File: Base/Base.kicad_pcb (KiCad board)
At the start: 2 copper layers, 23 parts, among them P1 CONN_01X02, P2 CONN_01X05, P3 CONN_01X08, P4 CONN_01X08, Q1 FDC606P, U1 tps610981, U2 M24M01, U4 CYBLE-022001-00

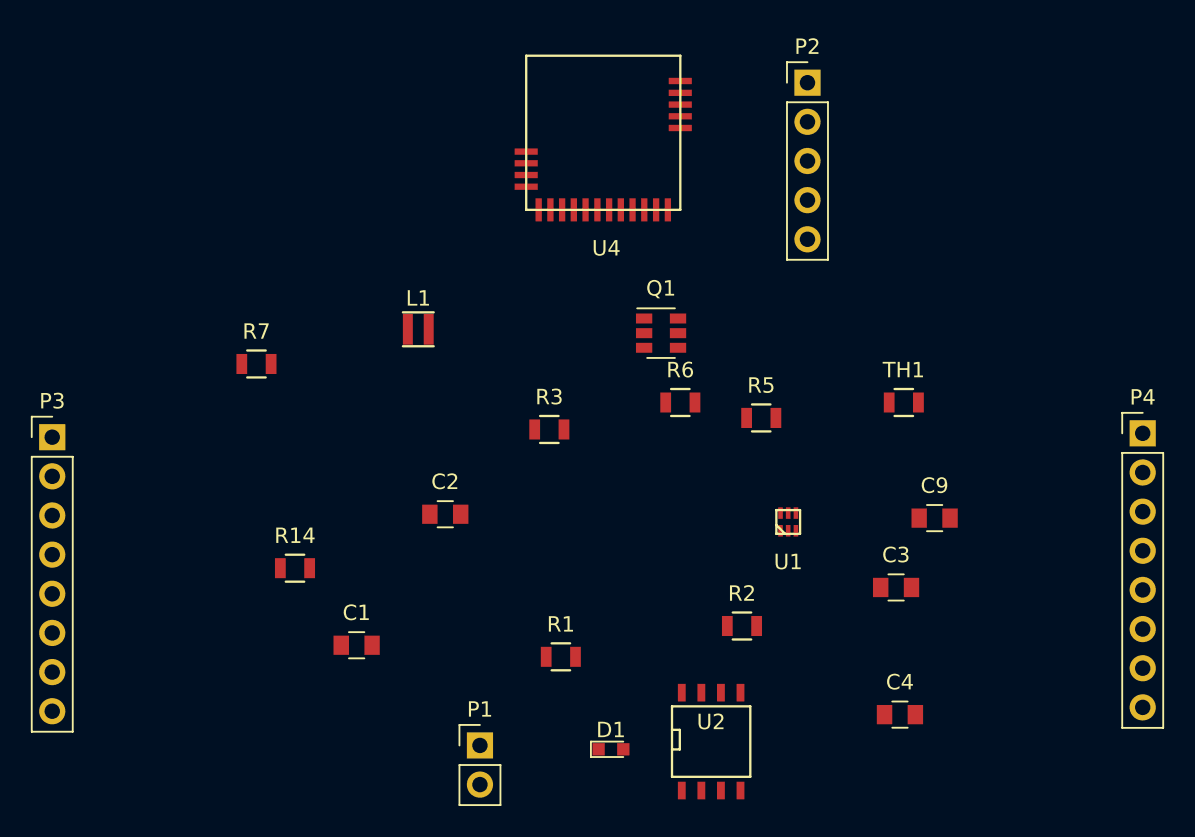
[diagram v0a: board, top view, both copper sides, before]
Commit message: Working on the layout for the base station.
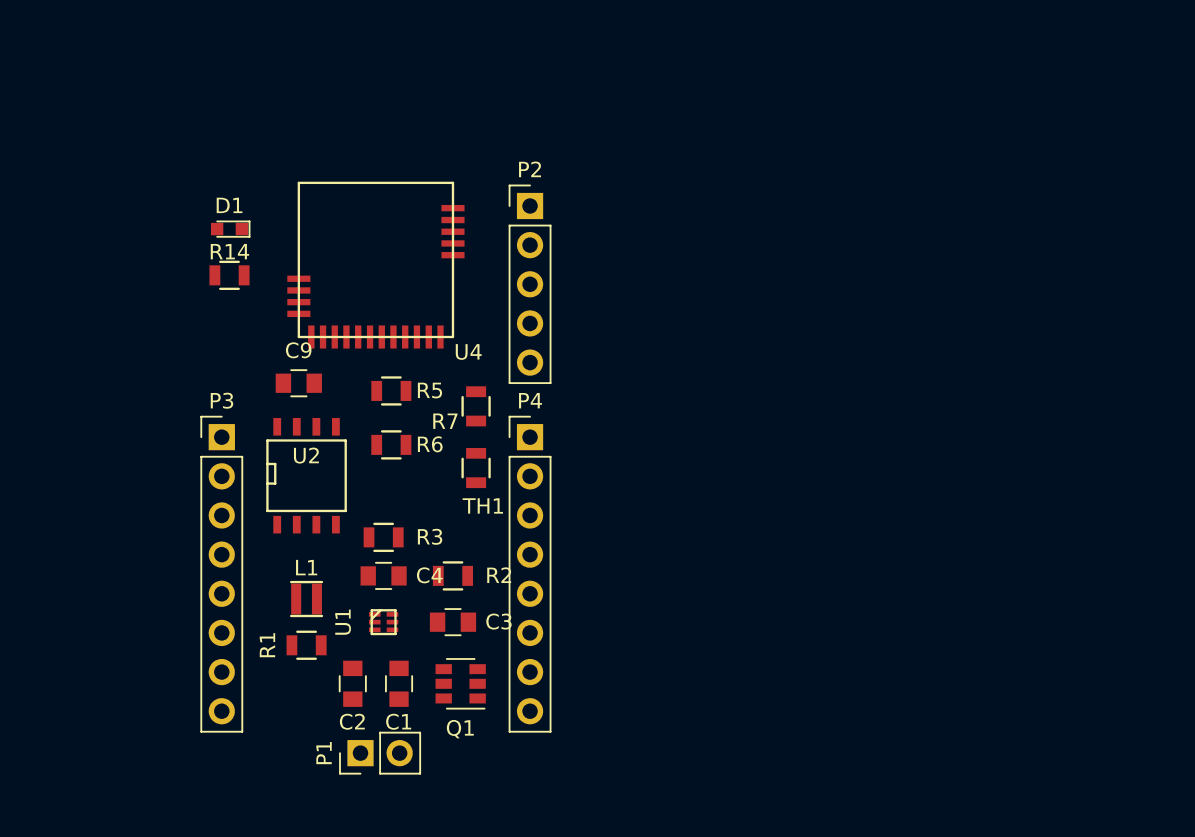
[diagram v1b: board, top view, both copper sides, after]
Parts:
- moved C9 42.2 mm to (124.0, 98.5)
- moved D1 41.9 mm to (119.5, 88.5), turned to 180 degrees
- moved P4 39.8 mm to (139.0, 102.0)
- moved C4 34.7 mm to (129.5, 111.0)
- moved U2 31.4 mm to (124.5, 104.5)
- moved C3 28.8 mm to (134.0, 114.0)
- moved TH1 28.1 mm to (135.5, 104.0), turned to 270 degrees
- moved U1 27.0 mm to (129.5, 114.0), turned to 270 degrees
- moved Q1 26.2 mm to (134.5, 118.0), turned to 180 degrees
- moved R5 24.1 mm to (130.0, 99.0), turned to 180 degrees
- moved P2 19.7 mm to (139.0, 87.0)
- moved R14 19.5 mm to (119.5, 91.5)
- moved R2 19.0 mm to (134.0, 111.0), turned to 180 degrees
- moved R6 19.0 mm to (130.0, 102.5), turned to 180 degrees
- moved L1 18.9 mm to (124.5, 112.5)
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
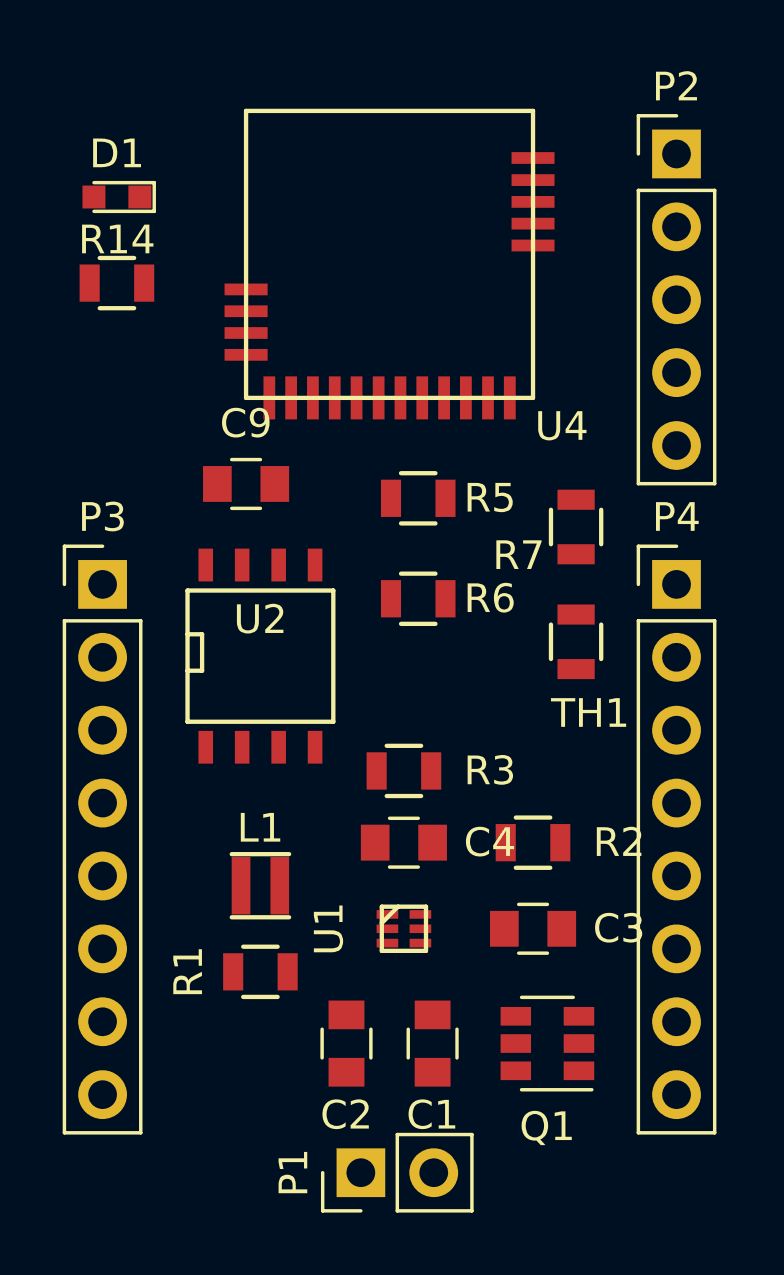
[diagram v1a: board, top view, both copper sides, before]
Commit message: Completed the routing.
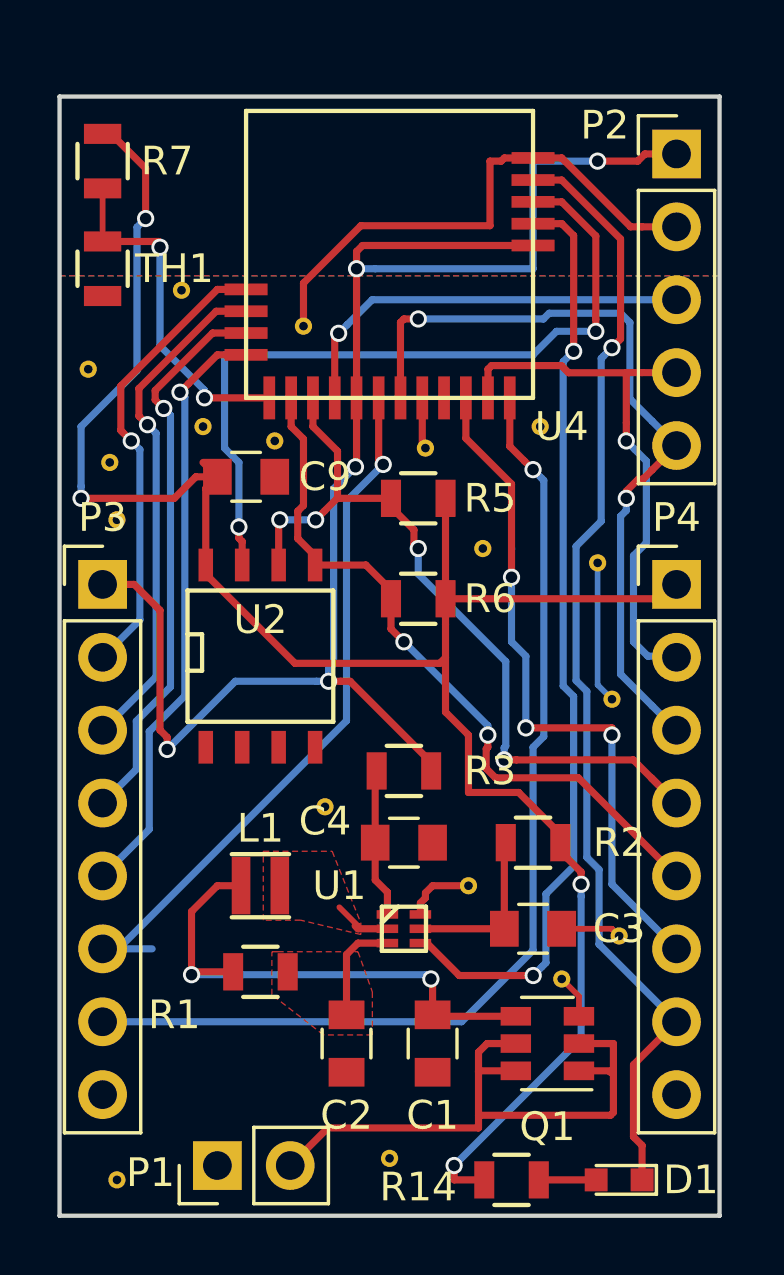
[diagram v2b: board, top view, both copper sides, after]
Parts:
- added REF**: via_0.3mm, KicadFootprint:via_0.3mm, F.Cu at (119.5, 99.8)
- added REF**: via_0.3mm, KicadFootprint:via_0.3mm, F.Cu at (136.2, 101.2)
- added REF**: via_0.3mm, KicadFootprint:via_0.3mm, F.Cu at (136.8, 106.0)
- added REF**: via_0.3mm, KicadFootprint:via_0.3mm, F.Cu at (132.2, 100.8)
- added REF**: via_0.3mm, KicadFootprint:via_0.3mm, F.Cu at (126.8, 109.8)
- added REF**: via_0.3mm, KicadFootprint:via_0.3mm, F.Cu at (137.0, 114.2)
- added REF**: via_0.3mm, KicadFootprint:via_0.3mm, F.Cu at (131.8, 112.5)
- added REF**: via_0.3mm, KicadFootprint:via_0.3mm, F.Cu at (135.0, 115.8)
- added REF**: via_0.3mm, KicadFootprint:via_0.3mm, F.Cu at (129.0, 122.0)
- added REF**: via_0.3mm, KicadFootprint:via_0.3mm, F.Cu at (119.5, 122.8)
- added REF**: via_0.3mm, KicadFootprint:via_0.3mm, F.Cu at (119.2, 97.8)
- added REF**: via_0.3mm, KicadFootprint:via_0.3mm, F.Cu at (121.8, 91.8)
- added REF**: via_0.3mm, KicadFootprint:via_0.3mm, F.Cu at (134.2, 96.5)
- added REF**: via_0.3mm, KicadFootprint:via_0.3mm, F.Cu at (126.0, 93.0)
- added REF**: via_0.3mm, KicadFootprint:via_0.3mm, F.Cu at (122.5, 96.5)
- added REF**: via_0.3mm, KicadFootprint:via_0.3mm, F.Cu at (125.0, 97.0)
- added REF**: via_0.3mm, KicadFootprint:via_0.3mm, F.Cu at (118.5, 94.5)
- added REF**: via_0.3mm, KicadFootprint:via_0.3mm, F.Cu at (130.2, 97.2)
- moved D1 38.5 mm to (137.0, 122.8)
- moved R14 34.1 mm to (133.2, 122.8), turned to 180 degrees
- moved TH1 21.0 mm to (119.0, 91.0)
- moved R7 20.9 mm to (119.0, 87.2)
- moved P1 5.01 mm to (123.0, 122.2)
- moved C9 0.25 mm to (124.0, 98.2)
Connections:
- P3 pad 2: /SWDIO -> /GPIO1
- P3 pad 3: /SWDCLK -> /ANALOG1
- P3 pad 4: /RX.MOSI -> /TX/MISO
- P3 pad 5: /TX/MISO -> /RX/MOSI
- P3 pad 6: /SS -> /SCLK
- P3 pad 7: /SCLK -> /SS
- P4 pad 2: /SDA -> /SWDCLK
- P4 pad 3: /SCL -> /SWDIO
- P4 pad 4: /ANALOG1 -> /SCL
- P4 pad 5: /ANALOG2 -> /SDA
- P4 pad 6: /GPIO1 -> /ANALOG2
- R7 pad 2: /ANALOG2 -> /TEMP
- TH1 pad 1: /ANALOG2 -> /TEMP
- U4 pad 17: /ANALOG2 -> /TEMP
- U4 pad 8: /GPIO2 -> /ANALOG2
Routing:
- net VDD: track 0.00 -> 71.6 mm, vias 0 -> 4
- net VCC: track 0.00 -> 55.7 mm, vias 0 -> 5
- net /LED: track 0.00 -> 39.5 mm, vias 0 -> 1
- net /SS: track 0.00 -> 35.9 mm, vias 0 -> 1
- net /PS_MODE: track 0.00 -> 32.7 mm, vias 0 -> 2
- net GND: track 0.00 -> 31.4 mm
- net /SWDIO: track 0.00 -> 27.5 mm, vias 0 -> 2
- net /SCL: track 0.00 -> 27.4 mm, vias 0 -> 4
- net /WP: track 0.00 -> 27.2 mm, vias 0 -> 2
- net /SDA: track 0.00 -> 25.5 mm, vias 0 -> 2
- net /SCLK: track 0.00 -> 25.4 mm, vias 0 -> 1
- net /ANALOG2: track 0.00 -> 24.0 mm, vias 0 -> 3
- net Net-(P1-Pad2): track 0.00 -> 22.2 mm
- net /RX/MOSI: track 0.00 -> 21.5 mm, vias 0 -> 1
- net /TX/MISO: track 0.00 -> 19.6 mm, vias 0 -> 1
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- added copper zone on B.Cu, net GND
- added copper zone on F.Cu, net GND
- added copper zone on F.Cu, net Net-(C2-Pad1)
- added copper zone on F.Cu, net Net-(L1-Pad2)
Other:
- board outline added: 23 x 39 mm
- net class Default: trace_width 0.25 -> 0.2

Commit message: Changing from a thermister ST LPS22HB pressure sensor.
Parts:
- removed R7: 10K, Resistors_SMD:R_0805
- removed the REF** at (119.5, 99.8)
- removed the REF** at (136.2, 101.2)
- removed the REF** at (136.8, 106.0)
- removed the REF** at (132.2, 100.8)
- removed the REF** at (126.8, 109.8)
- removed the REF** at (137.0, 114.2)
- removed the REF** at (131.8, 112.5)
- removed the REF** at (135.0, 115.8)
- removed the REF** at (129.0, 122.0)
- removed the REF** at (119.5, 122.8)
- removed the REF** at (119.2, 97.8)
- removed the REF** at (121.8, 91.8)
- removed the REF** at (134.2, 96.5)
- removed the REF** at (126.0, 93.0)
- removed the REF** at (122.5, 96.5)
- removed the REF** at (125.0, 97.0)
- removed the REF** at (118.5, 94.5)
- removed the REF** at (130.2, 97.2)
- removed TH1: Thermistor, Resistors_SMD:R_0805
- added REF**: via_0.3mm, KicadFootprint:via_0.3mm, F.Cu at (119.5, 92.0)
- added U3: LPS22HB, KicadFootprint:HLGA-10L, F.Cu at (120.5, 87.8)
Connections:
- U4 pad 17: /TEMP -> /INT_DRDY
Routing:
- net GND: track 31.4 -> 7.87 mm
- net /INT_DRDY: track 0.00 -> 18.0 mm, vias 0 -> 2
- net /TEMP: track 12.2 -> 0.00 mm, vias 2 -> 0
- net /SDA: track 25.5 -> 37.2 mm, vias 2 -> 4
- net /SCL: track 27.4 -> 38.4 mm, vias 4 -> 6
- net VDD: track 71.6 -> 79.5 mm
- net (no net): track 0.01 -> 4.97 mm

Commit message: Finished layout of SensorNode and FlowMeter boards.
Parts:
- added REF**: via_0.3mm, KicadFootprint:via_0.3mm, F.Cu at (132.2, 106.0)
- added REF**: via_0.3mm, KicadFootprint:via_0.3mm, F.Cu at (123.5, 104.5)
- added REF**: via_0.3mm, KicadFootprint:via_0.3mm, F.Cu at (137.0, 88.2)
- added REF**: via_0.3mm, KicadFootprint:via_0.3mm, F.Cu at (130.2, 97.2)
- added REF**: via_0.3mm, KicadFootprint:via_0.3mm, F.Cu at (124.0, 96.8)
- added REF**: via_0.3mm, KicadFootprint:via_0.3mm, F.Cu at (118.5, 87.5)
- added REF**: via_0.3mm, KicadFootprint:via_0.3mm, F.Cu at (121.5, 89.8)
- added REF**: via_0.3mm, KicadFootprint:via_0.3mm, F.Cu at (121.8, 86.2)
- added REF**: via_0.3mm, KicadFootprint:via_0.3mm, F.Cu at (132.2, 109.0)
- added REF**: via_0.3mm, KicadFootprint:via_0.3mm, F.Cu at (124.0, 119.2)
- added REF**: via_0.3mm, KicadFootprint:via_0.3mm, F.Cu at (129.0, 122.0)
- added REF**: via_0.3mm, KicadFootprint:via_0.3mm, F.Cu at (136.0, 121.2)
- added REF**: via_0.3mm, KicadFootprint:via_0.3mm, F.Cu at (137.0, 116.8)
- added REF**: via_0.3mm, KicadFootprint:via_0.3mm, F.Cu at (137.0, 113.8)
- added REF**: via_0.3mm, KicadFootprint:via_0.3mm, F.Cu at (132.0, 112.5)
- added REF**: via_0.3mm, KicadFootprint:via_0.3mm, F.Cu at (122.5, 109.8)
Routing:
- net GND: track 7.87 -> 34.4 mm, vias 0 -> 1
- net (no net): track 4.97 -> 0.01 mm
- net /SDA: track 37.2 -> 39.0 mm
- net /SCL: track 38.4 -> 37.1 mm
- net VDD: track 79.5 -> 80.8 mm
- net /INT_DRDY: track 18.0 -> 18.7 mm
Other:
- board text added: "SensorNode Rev A"
